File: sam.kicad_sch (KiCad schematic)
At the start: 59 parts, among them IC1 HYB4116, IC15 MC6883, IC16 74LS244N, IC2 HYB4116, IC3 HYB4116, IC31 74LS02N, IC33 74LS138N, IC4 HYB4116, IC5 HYB4116, IC6 HYB4116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

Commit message: update bom references
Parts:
- IC1, IC2, IC3, IC4, IC5, IC6, IC7, IC8: Mouser (none) -> 517-4816-3000-CP
- IC15: Mouser (none) -> 517-4840-6000-CP
- JP1-2: DigiKey 952-2521-ND -> (none); Mouser (none) -> 538-22-28-5033
- JP13-14, JP3-4, JP5-6, JP7-8: Mouser (none) -> 538-22-28-5033
- JP15/16, JP17/18: now left out of the parts list
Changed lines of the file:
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@@
 			)
 		)
+		(property "Mouser" "517-4816-3000-CP"
+			(at 35.433 42.418 0)
+			(effects
+				(font
+					(size 1.27 1.27)
+				)
+				(hide yes)
+			)
+		)
 		(pin "1"
 		)
@@
 			)
 		)
+		(property "Mouser" "538-22-28-5033"
+			(at 112.903 195.707 0)
+			(effects
+				(font
+					(size 1.27 1.27)
+				)
+				(hide yes)
+			)
+		)
 		(pin "1"
 		)
@@
 			)
 		)
+		(property "Mouser" "517-4816-3000-CP"
+			(at 120.777 42.545 0)
+			(effects
+				(font
+					(size 1.27 1.27)
+				)
+				(hide yes)
+			)
+		)
 		(pin "1"
 		)
@@
 		(unit 1)
 		(exclude_from_sim no)
-		(in_bom yes)
+		(in_bom no)
 		(on_board yes)
 		(dnp no)
@@
 			)
 		)
+		(property "Mouser" "538-22-28-5033"
+			(at 264.668 145.161 90)
+			(effects
+				(font
+					(size 1.27 1.27)
+				)
+				(hide yes)
+			)
+		)
 		(pin "1"
 		)
@@
 			)
 		)
+		(property "Mouser" "517-4816-3000-CP"
+			(at 78.105 42.418 0)
+			(effects
+				(font
+					(size 1.27 1.27)
+				)
+				(hide yes)
+			)
+		)
 		(pin "1"
 		)
@@
 			)
 		)
+		(property "Mouser" "517-4816-3000-CP"
+			(at 120.777 103.251 0)
+			(effects
+				(font
+					(size 1.27 1.27)
+				)
+				(hide yes)
+			)
+		)
 		(pin "1"
 		)
@@
 			)
 		)
-		(property "DigiKey" "952-2521-ND"
+		(property "DigiKey" ""
 			(at 248.92 117.983 0)
 			(effects
@@
 			)
 		)
+		(property "Mouser" "538-22-28-5033"
+			(at 248.92 117.983 90)
+			(effects
+				(font
+					(size 1.27 1.27)
+				)
+				(hide yes)
+			)
+		)
 		(pin "1"
 		)
@@
 			)
 		)
+		(property "Mouser" "517-4816-3000-CP"
+			(at 35.433 103.124 0)
+			(effects
+				(font
+					(size 1.27 1.27)
+				)
+				(hide yes)
+			)
+		)
 		(pin "1"
 		)
@@
 			)
 		)
+		(property "Mouser" "517-4816-3000-CP"
+			(at 163.449 103.251 0)
+			(effects
+				(font
+					(size 1.27 1.27)
+				)
+				(hide yes)
+			)
+		)
 		(pin "1"
 		)
@@
 		(unit 1)
 		(exclude_from_sim no)
-		(in_bom yes)
+		(in_bom no)
 		(on_board yes)
 		(dnp no)
@@
 			)
 		)
+		(property "Mouser" "517-4816-3000-CP"
+			(at 163.449 42.545 0)
+			(effects
+				(font
+					(size 1.27 1.27)
+				)
+				(hide yes)
+			)
+		)
 		(pin "1"
 		)
@@
 			)
 		)
+		(property "Mouser" "517-4816-3000-CP"
+			(at 78.105 103.124 0)
+			(effects
+				(font
+					(size 1.27 1.27)
+				)
+				(hide yes)
+			)
+		)
 		(pin "1"
 		)
@@
 			)
 		)
+		(property "Mouser" "538-22-28-5033"
+			(at 262.128 111.633 90)
+			(effects
+				(font
+					(size 1.27 1.27)
+				)
+				(hide yes)
+			)
+		)
 		(pin "1"
 		)
@@
 			)
 		)
+		(property "Mouser" "517-4840-6000-CP"
+			(at 244.856 60.071 0)
+			(effects
+				(font
+					(size 1.27 1.27)
+				)
+				(hide yes)
+			)
+		)
 		(pin "1"
 		)
@@
 			(effects
 				(font
+					(size 1.27 1.27)
+				)
+				(hide yes)
+			)
+		)
+		(property "Mouser" "538-22-28-5033"
+			(at 224.663 145.542 90)
+			(effects
+				(font

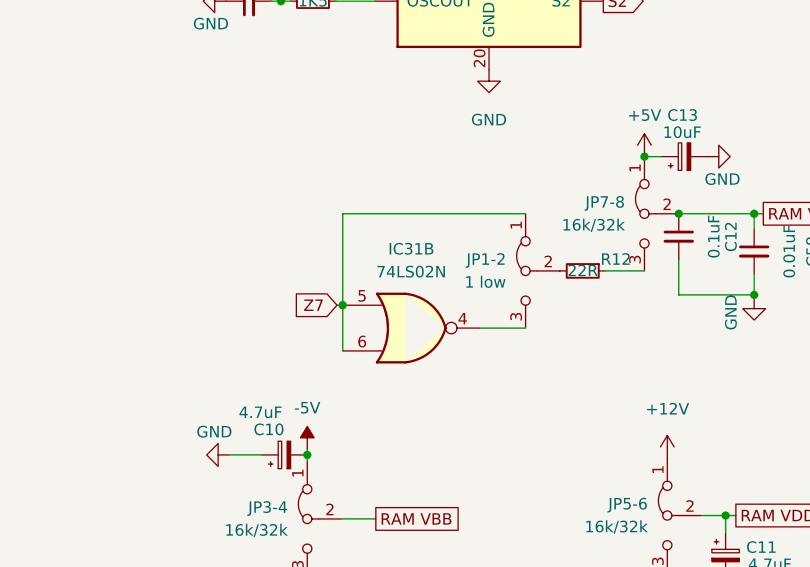
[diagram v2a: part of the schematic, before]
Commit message: fix parallel strobe inverter bypass
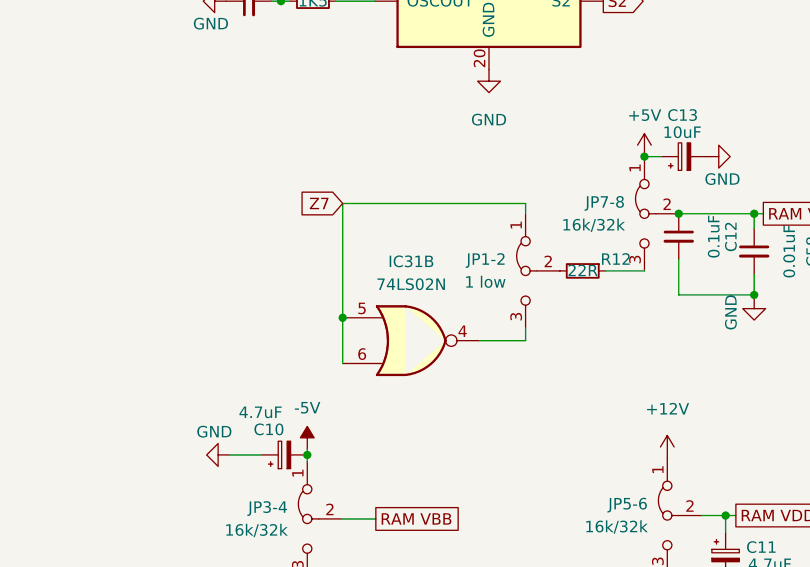
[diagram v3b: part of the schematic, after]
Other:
- company: (none) -> Dragon Data
- moved on the sheet: IC31B
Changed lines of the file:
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@@
 		(date "2023-06-03")
 		(rev "2.1")
+		(company "Dragon Data")
+		(comment 1 "Reproduced and Modified by Julian Brown")
 	)
 	(junction
@@
 	)
 	(junction
-		(at 228.6 121.793)
+		(at 228.6 123.19)
 		(diameter 0)
 		(color 0 0 0 0)
@@
 	(wire
 		(pts
-			(xy 228.6 121.793) (xy 228.6 111.633)
+			(xy 89.027 120.904) (xy 88.392 120.904)
 		)
 		(stroke
@@
 	(wire
 		(pts
-			(xy 89.027 120.904) (xy 88.392 120.904)
+			(xy 88.392 120.904) (xy 88.265 120.904)
 		)
 		(stroke
@@
 	(wire
 		(pts
-			(xy 88.392 120.904) (xy 88.265 120.904)
+			(xy 24.257 82.423) (xy 24.257 85.344)
 		)
 		(stroke
@@
 	(wire
 		(pts
-			(xy 24.257 82.423) (xy 24.257 85.344)
+			(xy 109.601 82.55) (xy 109.601 85.471)
 		)
 		(stroke
@@
 	(wire
 		(pts
-			(xy 109.601 82.55) (xy 109.601 85.471)
+			(xy 89.789 193.167) (xy 91.313 193.167)
 		)
 		(stroke
@@
 	(wire
 		(pts
-			(xy 89.789 193.167) (xy 91.313 193.167)
+			(xy 248.92 110.49) (xy 248.92 111.633)
 		)
 		(stroke
@@
 	(wire
 		(pts
-			(xy 228.6 111.633) (xy 248.92 111.633)
+			(xy 228.6 110.49) (xy 248.92 110.49)
 		)
 		(stroke
@@
 	(wire
 		(pts
+			(xy 248.92 125.73) (xy 248.92 124.333)
+		)
+		(stroke
+			(width 0)
+			(type default)
+		)
+	)
+	(wire
+		(pts
 			(xy 112.903 185.42) (xy 112.903 191.897)
 		)
@@
 	(wire
 		(pts
+			(xy 228.6 110.49) (xy 228.6 123.19)
+		)
+		(stroke
+			(width 0)
+			(type default)
+		)
+	)
+	(wire
+		(pts
 			(xy 46.355 120.904) (xy 45.72 120.904)
 		)
@@
 	(wire
 		(pts
-			(xy 248.92 124.333) (xy 243.84 124.333)
+			(xy 248.92 125.73) (xy 243.84 125.73)
 		)
 		(stroke
@@
 	(wire
 		(pts
-			(xy 228.6 121.793) (xy 228.6 126.873)
+			(xy 228.6 123.19) (xy 228.6 128.27)
 		)
 		(stroke
@@
 	(wire
 		(pts
-			(xy 227.965 121.793) (xy 228.6 121.793)
-		)
-		(stroke
-			(width 0)
-			(type default)
-		)
-	)
-	(wire
-		(pts
 			(xy 265.938 29.591) (xy 262.636 29.591)
 		)
@@
 	(global_label "Z7"
 		(shape input)
-		(at 227.965 121.793 180)
+		(at 228.6 110.49 180)
 		(fields_autoplaced yes)
 		(effects
@@
 		)
 		(property "Intersheetrefs" "${INTERSHEET_REFS}"
-			(at 223.2218 121.7136 0)
+			(at 223.8568 110.4106 0)
 			(effects
 				(font
@@
 	(symbol
 		(lib_id "74xx:74LS02")
-		(at 236.22 124.333 0)
+		(at 236.22 125.73 0)
 		(unit 2)
 		(exclude_from_sim no)
@@
 		(fields_autoplaced yes)
 		(property "Reference" "IC31"
-			(at 236.22 115.57 0)
+			(at 236.22 116.967 0)
 			(effects
 				(font
@@
 		)
 		(property "Value" "74LS02N"
-			(at 236.22 118.11 0)
+			(at 236.22 119.507 0)
 			(effects
 				(font
@@
 		)
 		(property "Footprint" "Package_DIP:DIP-14_W7.62mm"
-			(at 236.22 124.333 0)
+			(at 236.22 125.73 0)
 			(effects
 				(font
@@
 		)
 		(property "Datasheet" "http://www.ti.com/lit/gpn/sn74ls02"
-			(at 236.22 124.333 0)
+			(at 236.22 125.73 0)
 			(effects
 				(font
@@
 		)
 		(property "Description" ""
-			(at 236.22 124.333 0)
+			(at 236.22 125.73 0)
 			(effects
 				(font
@@
 		)
 		(property "DigiKey" "296-1627-5-ND"
-			(at 236.22 124.333 0)
+			(at 236.22 125.73 0)
 			(effects
 				(font
@@
 		)
 		(property "SA2120" "Sheet 1"
-			(at 236.22 124.333 0)
+			(at 236.22 125.73 0)
 			(effects
 				(font
